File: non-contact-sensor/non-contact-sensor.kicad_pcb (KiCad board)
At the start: 2 copper layers, 56.4 x 16 mm, 19 parts, among them J1 Conn_01x02, Q1 2N3904, U1 4011, U2 4011, U3 74LVC

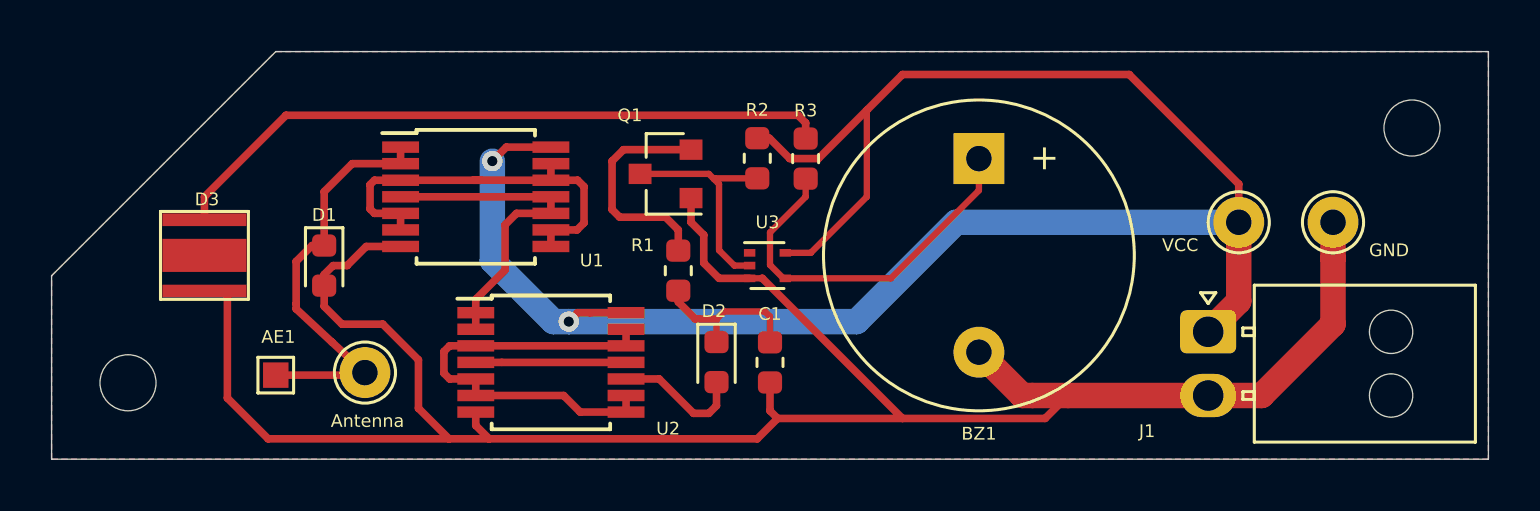
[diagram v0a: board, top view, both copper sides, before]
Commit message: Added a parts list, updated with parts for non-contact AC voltage sensor. Started work on front-end circuit, which will be used for controlling both input from manual buttons and a monochrome eInk screen.
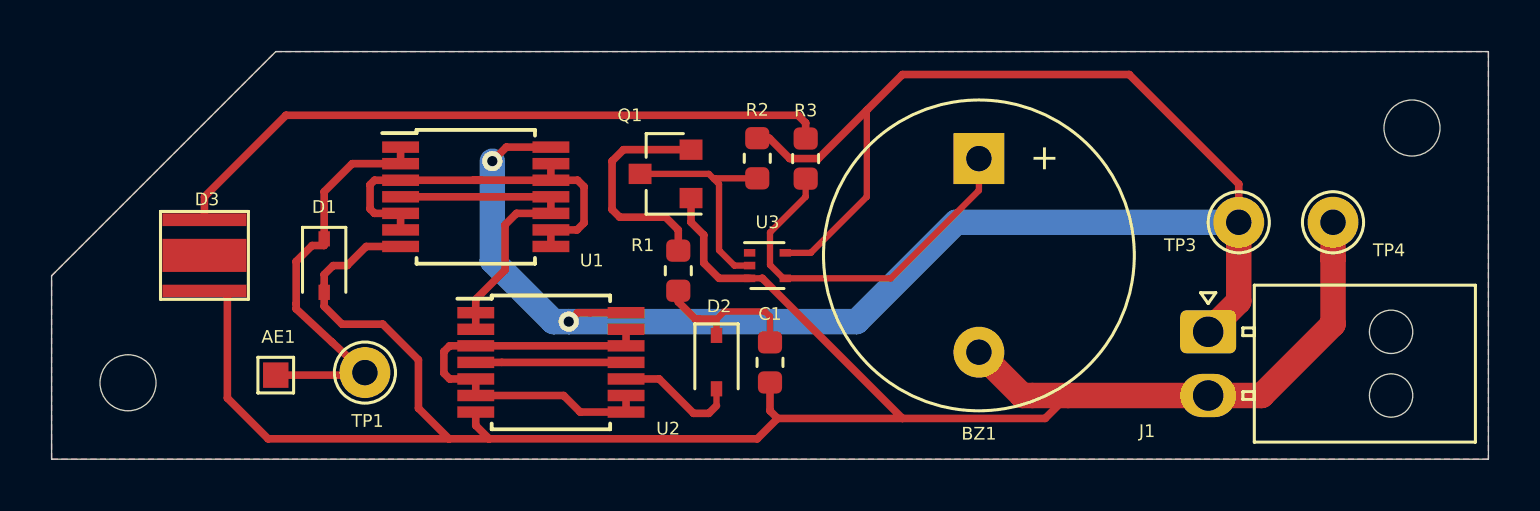
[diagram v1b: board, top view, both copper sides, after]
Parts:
- D1, D2: footprint Diode_SMD:D_0603_1608Metric -> Diode_SMD:D_SOD-323
- renumbered Antenna to TP1, VCC to TP3, GND to TP4
